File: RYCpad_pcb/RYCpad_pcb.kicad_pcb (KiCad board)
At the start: 2 copper layers, 77.2 x 117.6 mm, 71 parts, among them J1 USB_C_Receptacle_USB2.0, J2 AVR ISP, K1 KEYSW, K10 KEYSW, K11 KEYSW, K12 KEYSW, K13 KEYSW, K14 KEYSW, K15 KEYSW, K16 KEYSW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

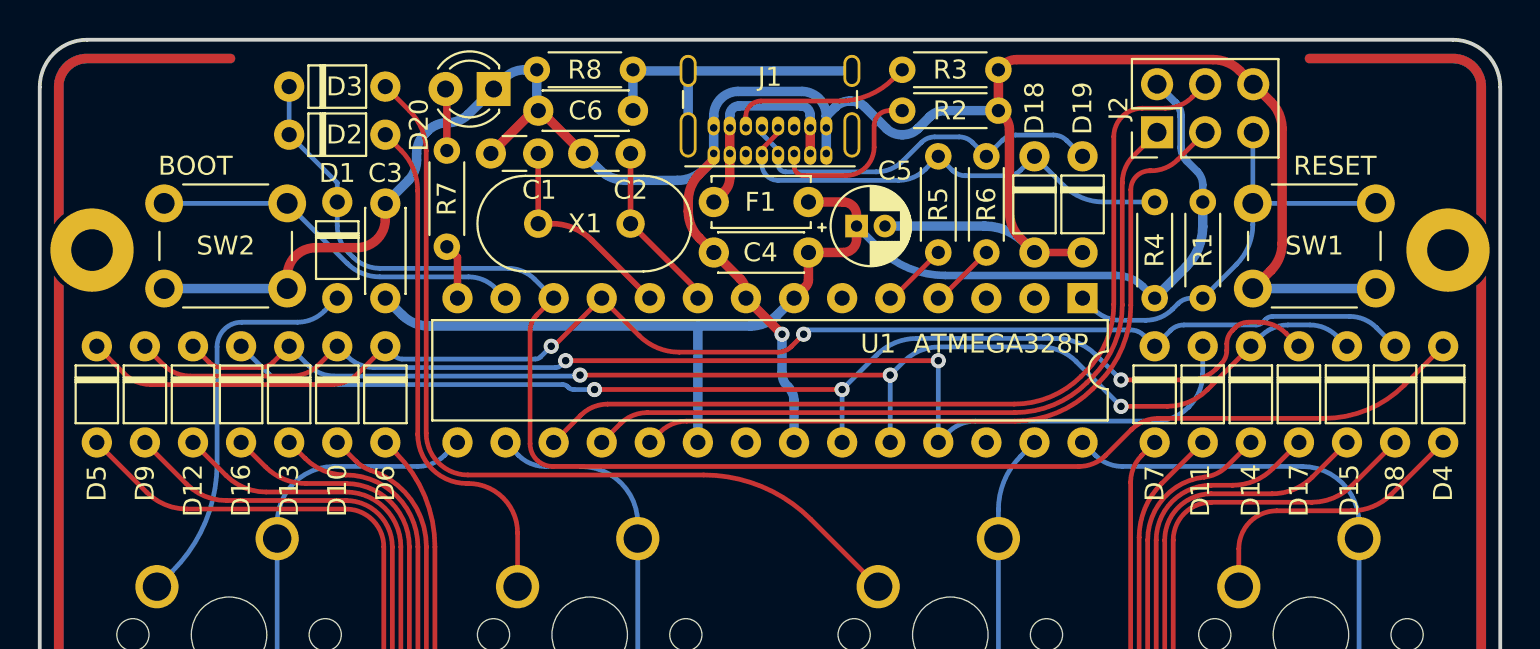
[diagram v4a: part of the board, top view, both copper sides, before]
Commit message: aesthetic changes
- Changed diode footprint to use prettier diode symbol
- Minor layout adjustments
- render update to follow in later commit
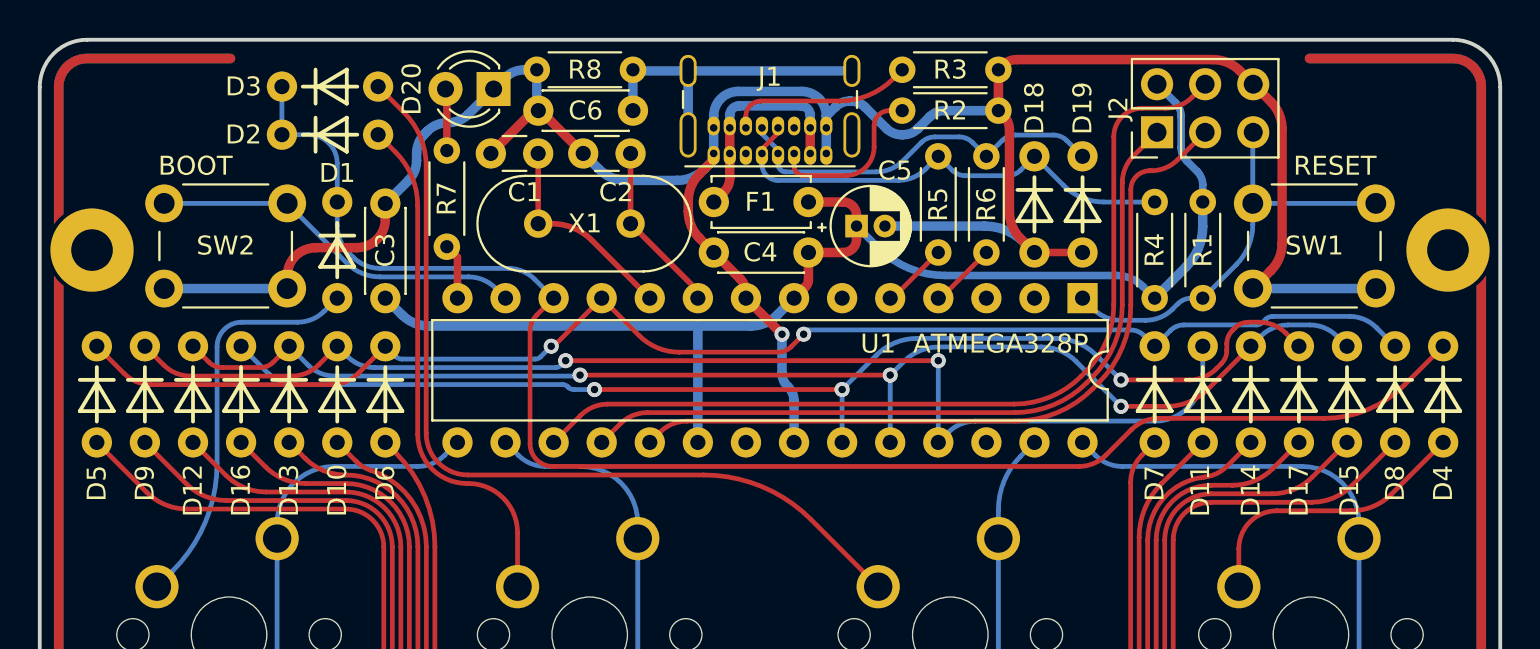
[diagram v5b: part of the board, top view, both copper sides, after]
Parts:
- moved D2 0.38 mm to (-25.8, -55.0)
- moved D3 0.38 mm to (-25.8, -57.5)
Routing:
- net /row0: track 81.2 -> 82.4 mm

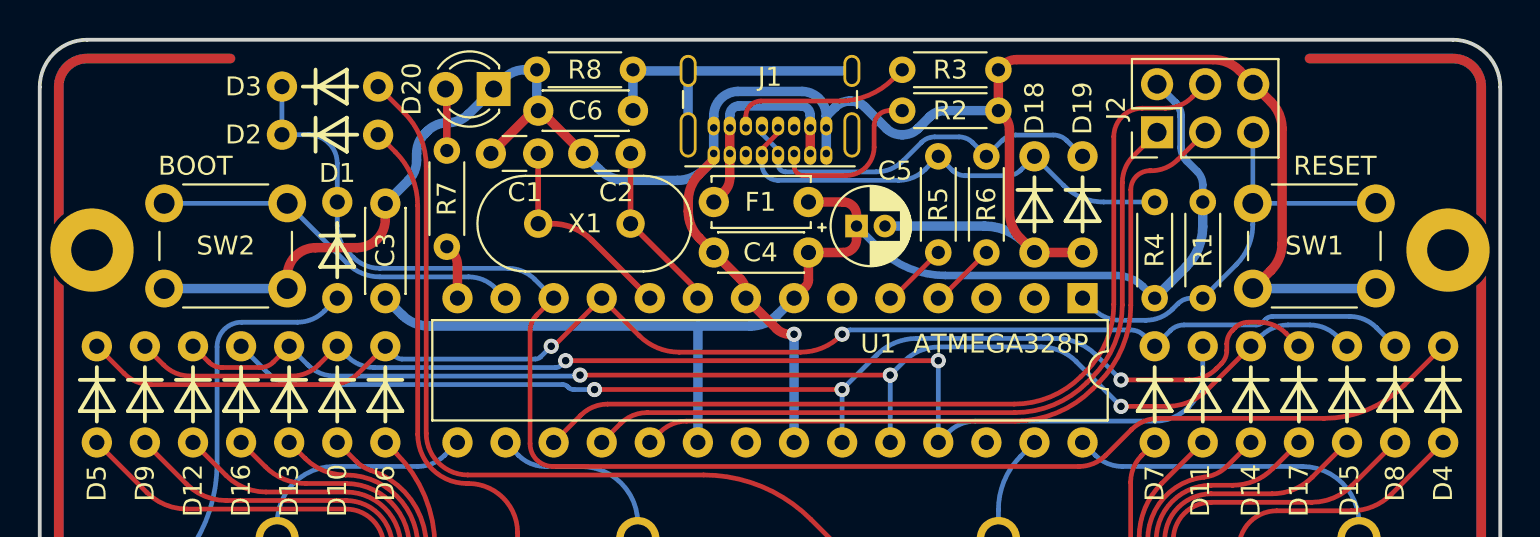
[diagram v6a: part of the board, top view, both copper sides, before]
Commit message: minor changes
- update rear pcb
- thinner silkscreen lines on diode footprint
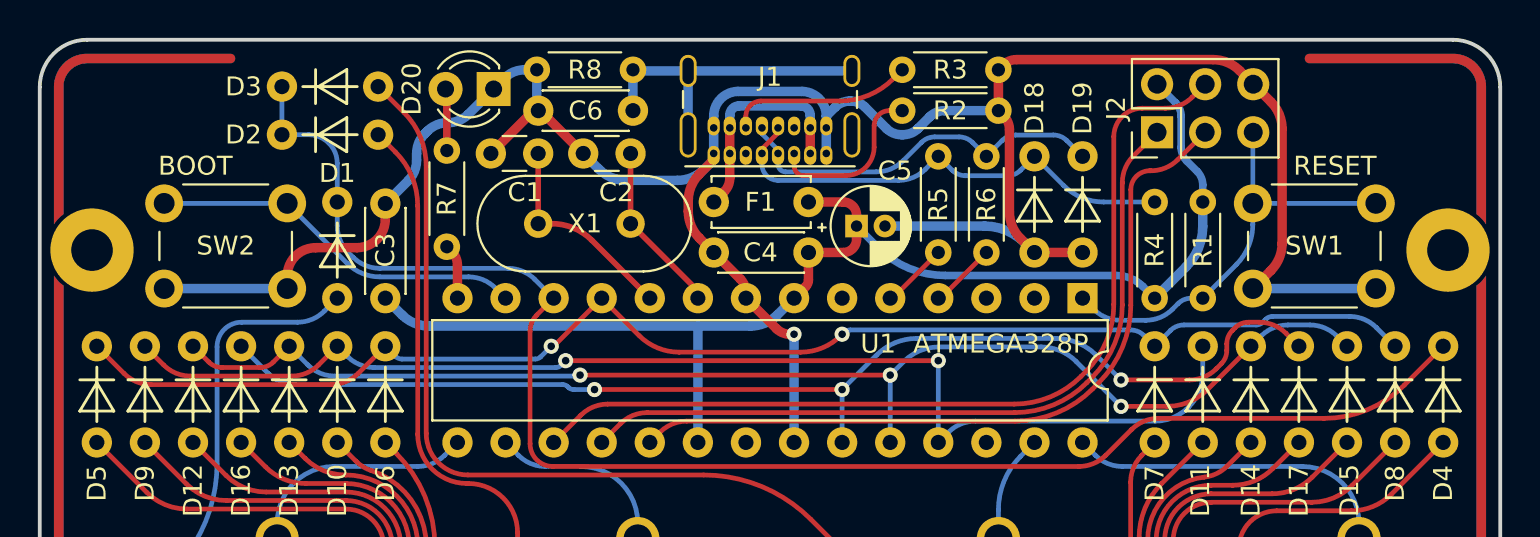
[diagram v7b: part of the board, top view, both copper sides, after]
